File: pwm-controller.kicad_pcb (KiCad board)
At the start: 2 copper layers, 49.5 x 36.8 mm, 32 parts, among them J1 POWER, J2 LOW SIDE, J3 CTRL, J4 POWER, J5 LOW SIDE, Q1 AO3400A, Q2 AO3400A, Q3 AO3400A, Q4 AO3400A, Q5 AO3400A, Q6 AO3400A, Q7 AO3400A, U1 L78L12_SOT89, U2 MCP1416

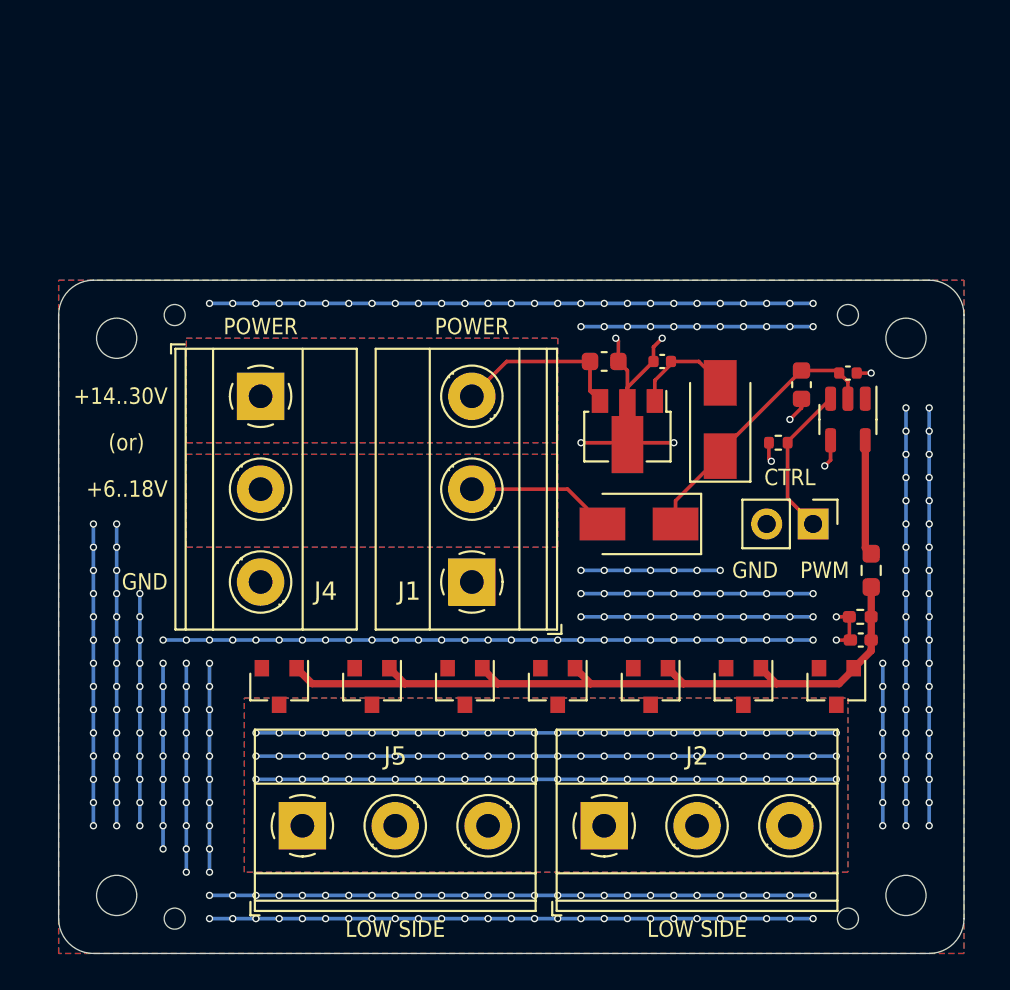
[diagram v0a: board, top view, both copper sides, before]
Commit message: ready, but some cost-saving opportunities left
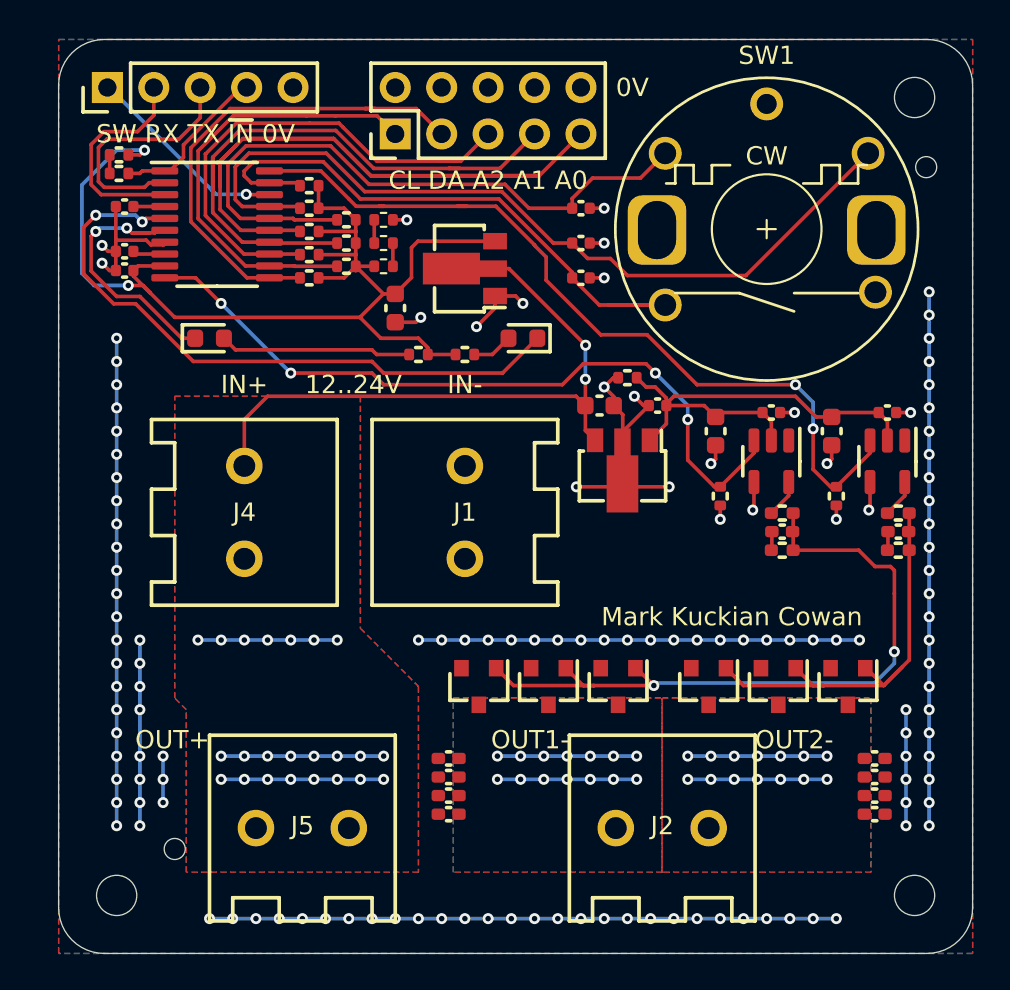
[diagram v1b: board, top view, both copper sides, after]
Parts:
- removed H3, H7: JLC, mark:JLCPCB_ToolingHole_1152_1300_1400_1650
- removed H6, H8: M2, MountingHole:MountingHole_2.2mm_M2
- removed J3: CTRL, Connector_PinHeader_2.54mm:PinHeader_1x02_P2.54mm_Vertical
- removed Q7: AO3400A, Package_TO_SOT_SMD:SOT-23
- added C10: 1u/50, Capacitor_SMD:C_0603_1608Metric, F.Cu at (117.9, 118.7)
- added C11: 100n/50, Capacitor_SMD:C_0402_1005Metric, F.Cu at (120.9, 117.7)
- added C12: 100n/50, Capacitor_SMD:C_0402_1005Metric_Pad0.74x0.62mm_HandSolder, F.Cu at (121.5, 124.2)
- added C13: 100n/50, Capacitor_SMD:C_0402_1005Metric_Pad0.74x0.62mm_HandSolder, F.Cu at (126.6, 139.7)
- added C14: 100n/50, Capacitor_SMD:C_0402_1005Metric_Pad0.74x0.62mm_HandSolder, F.Cu at (126.6, 138.7)
- added C15: 100n/50, Capacitor_SMD:C_0402_1005Metric_Pad0.74x0.62mm_HandSolder, F.Cu at (126.6, 137.7)
- added C16: 100n/50, Capacitor_SMD:C_0402_1005Metric_Pad0.74x0.62mm_HandSolder, F.Cu at (126.6, 136.7)
- added C17: 100n/50, Capacitor_SMD:C_0402_1005Metric_Pad0.74x0.62mm_HandSolder, F.Cu at (103.3, 136.7)
- added C18: 100n/50, Capacitor_SMD:C_0402_1005Metric_Pad0.74x0.62mm_HandSolder, F.Cu at (103.3, 137.7)
- added C19: 100n/50, Capacitor_SMD:C_0402_1005Metric_Pad0.74x0.62mm_HandSolder, F.Cu at (103.3, 138.7)
- added C20: 100n/50, Capacitor_SMD:C_0402_1005Metric_Pad0.74x0.62mm_HandSolder, F.Cu at (103.3, 139.7)
- added C21: 3.3n, Capacitor_SMD:C_0402_1005Metric, F.Cu at (110.5, 106.6)
- added C22: 3.3n, Capacitor_SMD:C_0402_1005Metric, F.Cu at (110.5, 108.5)
- added C23: 3.3n, Capacitor_SMD:C_0402_1005Metric, F.Cu at (110.5, 110.4)
- added C6: 3.3n, Capacitor_SMD:C_0402_1005Metric, F.Cu at (85.5, 108.9)
- added C7: 100n/50, Capacitor_SMD:C_0402_1005Metric, F.Cu at (85.5, 106.5)
- added C8: 100n/50, Capacitor_SMD:C_0402_1005Metric, F.Cu at (85.5, 110.0)
- added C9: 1u/50, Capacitor_SMD:C_0603_1608Metric, F.Cu at (100.3, 112.0)
- added H4: M2, MountingHole:MountingHole_2.2mm_M2, F.Cu at (128.7, 100.5)
- added J6: DEBUG, Connector_PinHeader_2.54mm:PinHeader_1x05_P2.54mm_Vertical, F.Cu at (84.6, 99.9)
- added J7: I2C, Connector_PinHeader_2.54mm:PinHeader_2x05_P2.54mm_Vertical, F.Cu at (100.3, 102.5)
- added R10: 4.7k, Resistor_SMD:R_0402_1005Metric, F.Cu at (95.6, 105.3)
- added R11: 4.7k, Resistor_SMD:R_0402_1005Metric, F.Cu at (95.6, 107.8)
- added R12: 120, Resistor_SMD:R_0402_1005Metric, F.Cu at (99.7, 109.7)
- added R13: 4.7k, Resistor_SMD:R_0402_1005Metric, F.Cu at (85.2, 104.6)
- added R14: 4.7k, Resistor_SMD:R_0402_1005Metric, F.Cu at (85.2, 103.6)
- added R15: 120, Resistor_SMD:R_0402_1005Metric, F.Cu at (104.1, 114.6)
- added R16: 120, Resistor_SMD:R_0402_1005Metric, F.Cu at (101.6, 114.6)
- added R17: 120, Resistor_SMD:R_0402_1005Metric_Pad0.72x0.64mm_HandSolder, F.Cu at (121.5, 123.2)
- added R18: 4.7k, Resistor_SMD:R_0402_1005Metric, F.Cu at (118.1, 122.3)
- added R19: 4.7k, Resistor_SMD:R_0402_1005Metric_Pad0.72x0.64mm_HandSolder, F.Cu at (121.5, 125.3)
- added R20: 4.7k, Resistor_SMD:R_0402_1005Metric, F.Cu at (113.0, 115.8)
- added R21: 120, Resistor_SMD:R_0402_1005Metric, F.Cu at (99.7, 108.5)
- added R22: 120, Resistor_SMD:R_0402_1005Metric, F.Cu at (99.7, 107.2)
- added R4: 4.7k, Resistor_SMD:R_0402_1005Metric, F.Cu at (97.7, 109.7)
- added R5: 4.7k, Resistor_SMD:R_0402_1005Metric, F.Cu at (95.6, 110.4)
- added R6: 4.7k, Resistor_SMD:R_0402_1005Metric, F.Cu at (97.7, 107.2)
- added R7: 4.7k, Resistor_SMD:R_0402_1005Metric, F.Cu at (95.6, 109.1)
- added R8: 4.7k, Resistor_SMD:R_0402_1005Metric, F.Cu at (95.6, 106.6)
- added R9: 4.7k, Resistor_SMD:R_0402_1005Metric, F.Cu at (97.7, 108.5)
- added SW1: EC12D1524403, mark:RotaryEncoder_Alps_EC12D_Vertical_H20mm_easy, F.Cu at (120.7, 107.7)
- added U3: STM8S003F3Px, Package_SO:TSSOP-20_4.4x6.5mm_P0.65mm, F.Cu at (90.6, 107.4)
- added U4: HT7533-1-SOT89, Package_TO_SOT_SMD:SOT-89-3, F.Cu at (104.1, 109.9)
- added U5: MCP1416, Package_TO_SOT_SMD:SOT-23-5, F.Cu at (120.9, 120.4)
- C5: value 10n -> 100n/50
- D1: value Schottky -> Green; footprint Diode_SMD:D_SMA -> LED_SMD:LED_0603_1608Metric
- D2: value Schottky -> Blue; footprint Diode_SMD:D_SMA -> LED_SMD:LED_0603_1608Metric
- J1: value POWER -> IN-; footprint TerminalBlock_Phoenix:TerminalBlock_Phoenix_MKDS-1,5-3-5.08_1x03_P5.08mm_Horizontal -> mark:ScrewTerminal_5.08P_1x02_10.16x10.16mm
- J2: value LOW SIDE -> OUT-; footprint TerminalBlock_Phoenix:TerminalBlock_Phoenix_MKDS-1,5-3-5.08_1x03_P5.08mm_Horizontal -> mark:ScrewTerminal_5.08P_1x02_10.16x10.16mm
- J4: value POWER -> IN+; footprint TerminalBlock_Phoenix:TerminalBlock_Phoenix_MKDS-1,5-3-5.08_1x03_P5.08mm_Horizontal -> mark:ScrewTerminal_5.08P_1x02_10.16x10.16mm
- J5: value LOW SIDE -> OUT+; footprint TerminalBlock_Phoenix:TerminalBlock_Phoenix_MKDS-1,5-3-5.08_1x03_P5.08mm_Horizontal -> mark:ScrewTerminal_5.08P_1x02_10.16x10.16mm
- R1: value 4.7k -> 120; footprint Resistor_SMD:R_0402_1005Metric -> Resistor_SMD:R_0402_1005Metric_Pad0.72x0.64mm_HandSolder
- R2: value 100 -> 4.7k; footprint Resistor_SMD:R_0603_1608Metric_Pad0.98x0.95mm_HandSolder -> Resistor_SMD:R_0402_1005Metric
- U1: value L78L12_SOT89 -> L78L09_SOT89
- moved H1 41.9 mm to (129.4, 104.3)
- moved D2 28.3 mm to (90.2, 113.7), turned to 0 degrees
- moved D1 12.0 mm to (107.3, 113.7)
- moved R1 7.61 mm to (127.9, 123.2)
- moved J4 6.41 mm to (92.1, 123.2)
- moved C5 6.28 mm to (127.9, 124.2)
- moved Q6 5.84 mm to (104.9, 132.7)
- moved Q5 4.57 mm to (108.7, 132.7)
- moved R2 4.49 mm to (124.5, 122.3), turned to 270 degrees
- moved R3 4.20 mm to (127.9, 125.3), turned to 180 degrees
- moved J1 3.83 mm to (104.1, 123.2)
- moved H5 3.81 mm to (88.3, 141.6)
- moved Q4 3.30 mm to (112.5, 132.7)
- moved J2 3.18 mm to (114.9, 140.5)
- moved Q3 3.17 mm to (117.5, 132.7)
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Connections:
- C1 pad 1: /24VIN -> VIN
- C2 pad 1: Net-(C2-Pad1) -> +9V
- C3 pad 1: VDD -> +9V
- C4 pad 1: VDD -> +9V
- C5 pad 1: /GATE -> /channel1/GATE
- D1 pad 1: VDD -> LED1
- D1 pad 2: /12VIN -> Net-(D1-Pad2)
- D2 pad 1: VDD -> LED2
- D2 pad 2: Net-(C2-Pad1) -> Net-(D2-Pad2)
- J1 pad 2: /12VIN -> GND
- J2 pad 1: /DRAIN -> DRAIN2
- J2 pad 2: /DRAIN -> DRAIN1
- J4 pad 1: /24VIN -> VIN
- J4 pad 2: /12VIN -> VIN
- J5 pad 1: /DRAIN -> VIN
- J5 pad 2: /DRAIN -> VIN
- Q1 pad 1: /GATE -> /channel1/GATE
- Q1 pad 3: /DRAIN -> DRAIN1
- Q2 pad 1: /GATE -> /channel1/GATE
- Q2 pad 3: /DRAIN -> DRAIN1
- Q3 pad 1: /GATE -> /channel1/GATE
- Q3 pad 3: /DRAIN -> DRAIN1
- Q4 pad 1: /GATE -> /channel2/GATE
- Q4 pad 3: /DRAIN -> DRAIN2
- Q5 pad 1: /GATE -> /channel2/GATE
- Q5 pad 3: /DRAIN -> DRAIN2
- Q6 pad 1: /GATE -> /channel2/GATE
- Q6 pad 3: /DRAIN -> DRAIN2
- R1 pad 1: /CTRL -> /channel1/GATE
- R1 pad 2: GND -> /channel1/GATE_DRV
- R2 pad 1: /GATE -> PWM1
- R2 pad 2: /GATE_DRV -> GND
- R3 pad 1: GND -> /channel1/GATE
- R3 pad 2: /GATE -> GND
- U1 pad 1: Net-(C2-Pad1) -> +9V
- U1 pad 3: /24VIN -> VIN
- U2 pad 2: VDD -> +9V
- U2 pad 3: /CTRL -> PWM1
- U2 pad 5: /GATE_DRV -> /channel1/GATE_DRV
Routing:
- net GND: track 336.6 -> 175.6 mm, vias 274 -> 132
- net /DRAIN: track 95.2 -> 0.00 mm, vias 78 -> 0
- net +3V3: track 0.00 -> 62.0 mm, vias 0 -> 2
- net VIN: track 0.00 -> 59.6 mm, vias 0 -> 25
- net SADD0: track 0.00 -> 55.7 mm
- net RE_Q: track 0.00 -> 46.0 mm
- net PWM1: track 0.00 -> 45.3 mm, vias 0 -> 2
- net /GATE: track 42.1 -> 0.00 mm
- net PWM2: track 0.00 -> 41.3 mm, vias 0 -> 4
- net /channel2/GATE: track 0.00 -> 39.1 mm, vias 0 -> 2
- net RE_I: track 0.00 -> 35.9 mm
- net LED1: track 0.00 -> 35.3 mm, vias 0 -> 2
- net RE_B: track 0.00 -> 33.3 mm
- net SADD1: track 0.00 -> 32.8 mm
- net SADD2: track 0.00 -> 27.9 mm
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- added copper zone on B.Cu, net DRAIN1
- added copper zone on F.Cu, net DRAIN1
- added copper zone on B.Cu, net DRAIN2
- added copper zone on F.Cu, net DRAIN2
- added copper zone on B.Cu, net VIN
- added copper zone on F.Cu, net VIN
- removed copper zone on B.Cu, net /12VIN
- removed copper zone on F.Cu, net /12VIN
- removed copper zone on B.Cu, net /24VIN
- removed copper zone on F.Cu, net /24VIN
- removed copper zone on B.Cu, net /DRAIN
- removed copper zone on F.Cu, net /DRAIN
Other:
- board size 49.5 x 36.8 mm -> 50 x 50 mm
- net class Default: via_dia 0.4 -> 0.6; via_drill 0.25 -> 0.3
- net class Gate removed
- net class Power removed
- net class Signal removed
- rule via_min_drill: 0.25 -> 0.3
- rule via_min_size: 0.4 -> 0.6
- board text added: "0V"
- board text added: "10A should cause up to 100mV noise on GND. Slotting GND plane to reduce noise in digital section."
- board text added: "12..24V"
- board text added: "CL DA A2 A1 A0"
- board text added: "Mark Kuckian Cowan"
- board text added: "SW RX TX ~IN~ 0V"
- board text removed: "(or)"
- board text removed: "+14..30V"
- board text removed: "+6..18V"
- board text removed: "GND"
- board text removed: "PWM"

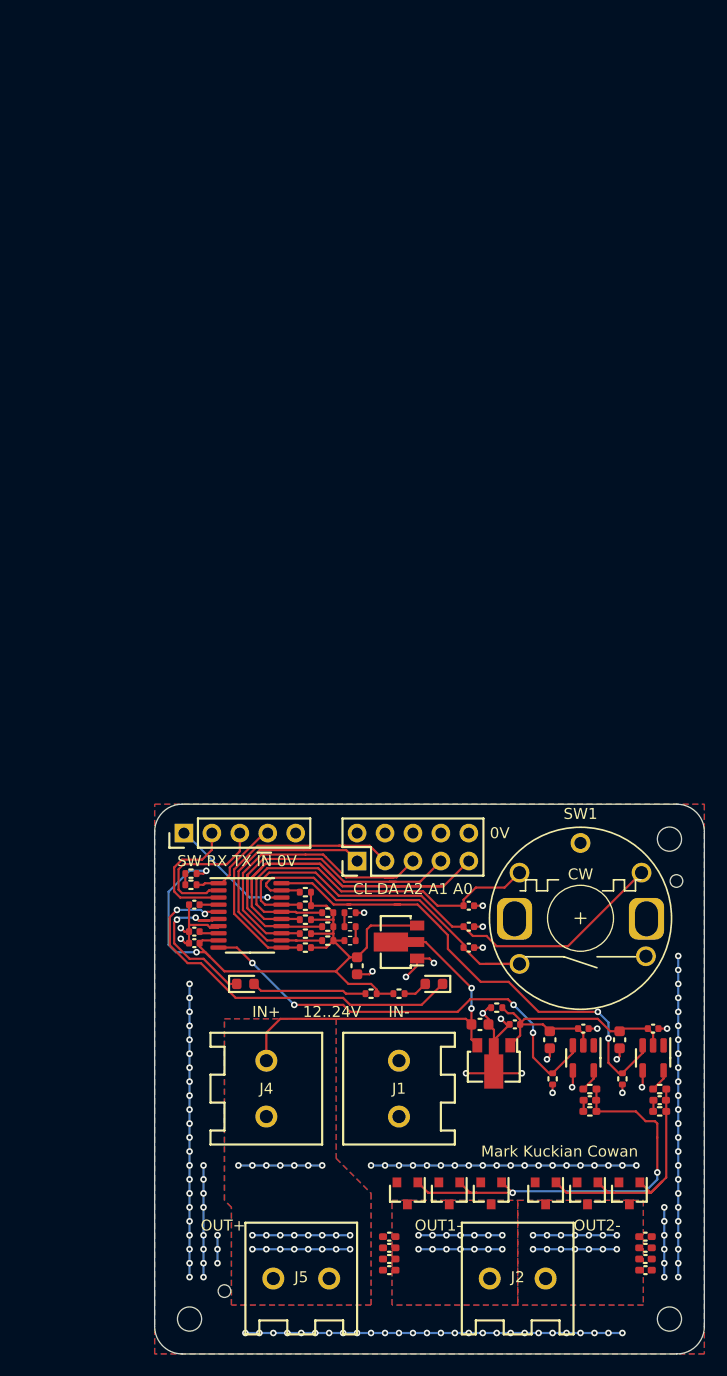
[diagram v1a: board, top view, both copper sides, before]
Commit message: dual channel, cheaper (jellybean gate driver)
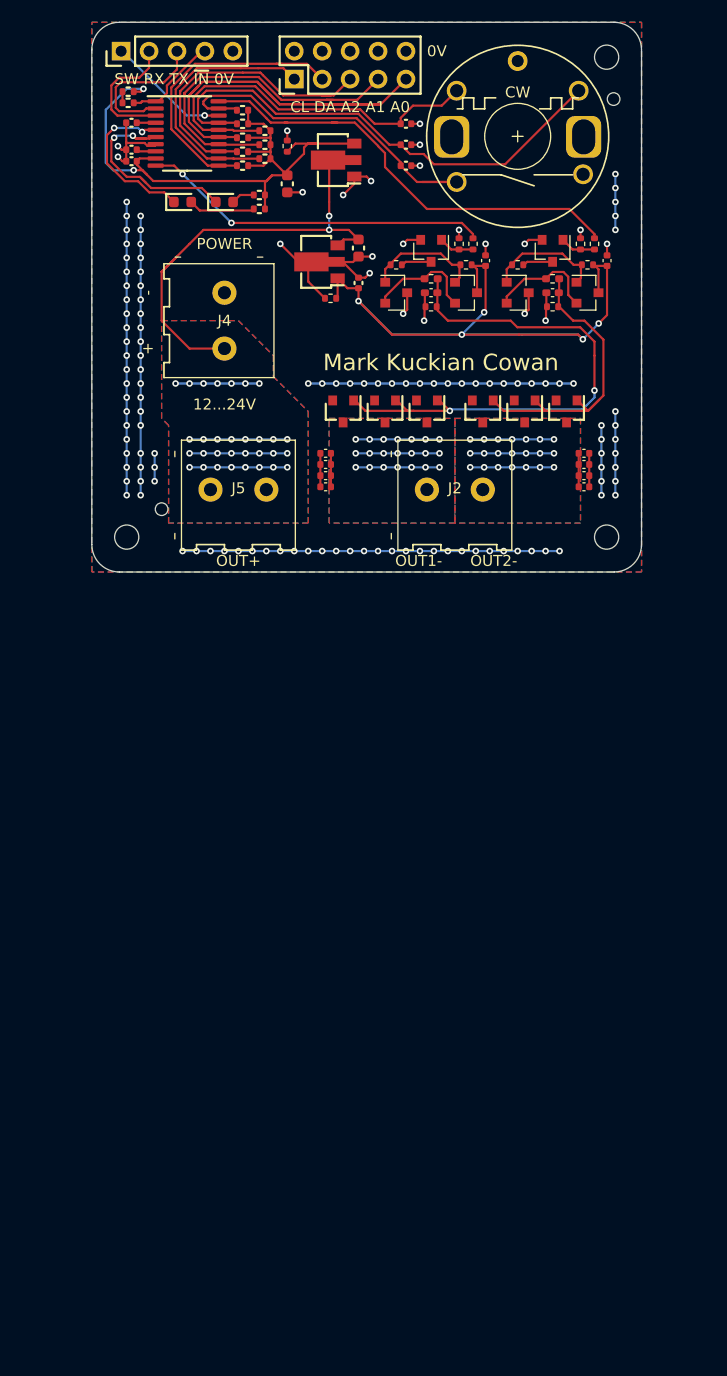
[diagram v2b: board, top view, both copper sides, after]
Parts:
- removed C11: 100n/50, Capacitor_SMD:C_0402_1005Metric
- removed C12: 100n/50, Capacitor_SMD:C_0402_1005Metric_Pad0.74x0.62mm_HandSolder
- removed J1: IN-, mark:ScrewTerminal_5.08P_1x02_10.16x10.16mm
- removed R21, R22: 120, Resistor_SMD:R_0402_1005Metric
- removed U2, U5: MCP1416, Package_TO_SOT_SMD:SOT-23-5
- added Q10: MMBT5551, Package_TO_SOT_SMD:SOT-23, F.Cu at (110.2, 50.8)
- added Q11: MMBT5551, Package_TO_SOT_SMD:SOT-23, F.Cu at (107.1, 47.0)
- added Q12: MMBT5401, Package_TO_SOT_SMD:SOT-23, F.Cu at (103.9, 50.8)
- added Q7: MMBT5551, Package_TO_SOT_SMD:SOT-23, F.Cu at (121.3, 50.8)
- added Q8: MMBT5551, Package_TO_SOT_SMD:SOT-23, F.Cu at (118.1, 47.0)
- added Q9: MMBT5401, Package_TO_SOT_SMD:SOT-23, F.Cu at (114.9, 50.8)
- added R23: 4.7k, Resistor_SMD:R_0402_1005Metric, F.Cu at (110.2, 48.3)
- added R24: 120, Resistor_SMD:R_0402_1005Metric_Pad0.72x0.64mm_HandSolder, F.Cu at (107.1, 49.5)
- added R25: 4.7k, Resistor_SMD:R_0402_1005Metric, F.Cu at (103.9, 48.3)
- added R27: 4.7k, Resistor_SMD:R_0402_1005Metric, F.Cu at (107.1, 52.1)
- added R28: 1k, Resistor_SMD:R_0402_1005Metric, F.Cu at (110.9, 46.4)
- added R29: 4.7k, Resistor_SMD:R_0402_1005Metric, F.Cu at (109.6, 46.4)
- C10: value 1u/50 -> 100n/50; footprint Capacitor_SMD:C_0603_1608Metric -> Capacitor_SMD:C_0402_1005Metric
- C13, C14, C15, C16, C17, C18, C19, C20, C5: footprint Capacitor_SMD:C_0402_1005Metric_Pad0.74x0.62mm_HandSolder -> Capacitor_SMD:C_0402_1005Metric
- C3: value 1u/50 -> 100n/50; footprint Capacitor_SMD:C_0603_1608Metric -> Capacitor_SMD:C_0402_1005Metric_Pad0.74x0.62mm_HandSolder
- C4: footprint Capacitor_SMD:C_0402_1005Metric -> Capacitor_SMD:C_0402_1005Metric_Pad0.74x0.62mm_HandSolder
- J4: value IN+ -> POWER
- R1, R17: value 120 -> 4.7k; footprint Resistor_SMD:R_0402_1005Metric_Pad0.72x0.64mm_HandSolder -> Resistor_SMD:R_0402_1005Metric
- R12: value 120 -> 4.7k
- R19: value 4.7k -> 1k; footprint Resistor_SMD:R_0402_1005Metric_Pad0.72x0.64mm_HandSolder -> Resistor_SMD:R_0402_1005Metric
- R2: value 4.7k -> 120; footprint Resistor_SMD:R_0402_1005Metric -> Resistor_SMD:R_0402_1005Metric_Pad0.72x0.64mm_HandSolder
- R3: footprint Resistor_SMD:R_0402_1005Metric_Pad0.72x0.64mm_HandSolder -> Resistor_SMD:R_0402_1005Metric
- moved R17 90.1 mm to (94.0, 37.5), turned to 270 degrees
- moved R19 78.9 mm to (121.9, 46.4), turned to 90 degrees
- moved R3 78.1 mm to (114.9, 48.3), turned to 0 degrees
- moved C5 78.0 mm to (112.0, 47.9), turned to 90 degrees
- moved R1 75.3 mm to (121.3, 48.3)
- moved D1 74.7 mm to (84.5, 42.5), turned to 0 degrees
- moved U1 74.6 mm to (96.9, 48.0), turned to 180 degrees
- moved R16 73.4 mm to (91.4, 41.9)
- moved R2 73.0 mm to (118.1, 49.5), turned to 0 degrees
- moved R15 72.5 mm to (91.4, 43.2), turned to 0 degrees
- moved J2 72.0 mm to (109.2, 68.7)
- moved J5 72.0 mm to (89.5, 68.7)
- moved C18 71.5 mm to (97.5, 66.4)
- moved C19 71.5 mm to (97.5, 67.4)
- moved C17 71.5 mm to (97.5, 65.4)
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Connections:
- C3 pad 1: +9V -> /channel1/GATE
- C4 pad 1: +9V -> /channel2/GATE
- C5 pad 1: /channel1/GATE -> +9V
- J4 pad 1: VIN -> GND
- R1 pad 1: /channel1/GATE -> +9V
- R1 pad 2: /channel1/GATE_DRV -> Net-(Q7-Pad1)
- R12 pad 1: Net-(R12-Pad1) -> GND
- R12 pad 2: +3V3 -> +9V
- R17 pad 1: /channel2/GATE -> GND
- R17 pad 2: /channel2/GATE_DRV -> +3V3
- R18 pad 1: PWM2 -> /channel1/GATE
- R19 pad 1: /channel2/GATE -> Net-(Q8-Pad1)
- R19 pad 2: GND -> PWM1
- R2 pad 1: PWM1 -> Net-(Q7-Pad2)
- R2 pad 2: GND -> /channel1/GATE
- R20 pad 1: GND -> Net-(Q8-Pad1)
- R20 pad 2: +9V -> GND
- R3 pad 1: /channel1/GATE -> Net-(Q7-Pad1)
- R3 pad 2: GND -> Net-(Q8-Pad3)
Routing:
- net +9V: track 26.4 -> 71.7 mm, vias 0 -> 5
- net LED1: track 35.3 -> 15.0 mm
- net VIN: track 59.6 -> 77.6 mm, vias 25 -> 33
- net GND: track 175.6 -> 190.3 mm, vias 132 -> 133
- net Net-(Q7-Pad1): track 0.00 -> 10.7 mm
- net Net-(Q10-Pad1): track 0.00 -> 10.7 mm
- net DRAIN2: track 15.2 -> 25.9 mm, vias 14 -> 21
- net DRAIN1: track 15.2 -> 25.9 mm, vias 14 -> 21
- net /channel2/GATE: track 39.1 -> 49.4 mm
- net Net-(Q10-Pad2): track 0.00 -> 10.0 mm
- net Net-(Q7-Pad2): track 0.00 -> 10.0 mm
- net PWM2: track 41.3 -> 31.8 mm, vias 4 -> 2
- net Net-(D2-Pad2): track 10.5 -> 2.14 mm
- net /channel1/GATE: track 23.8 -> 28.6 mm
- net LED2: track 14.6 -> 19.1 mm
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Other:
- board text removed: "12..24V"

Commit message: simulation provided many improvements, now aboutto switch to 5v single-rail for all control stuff
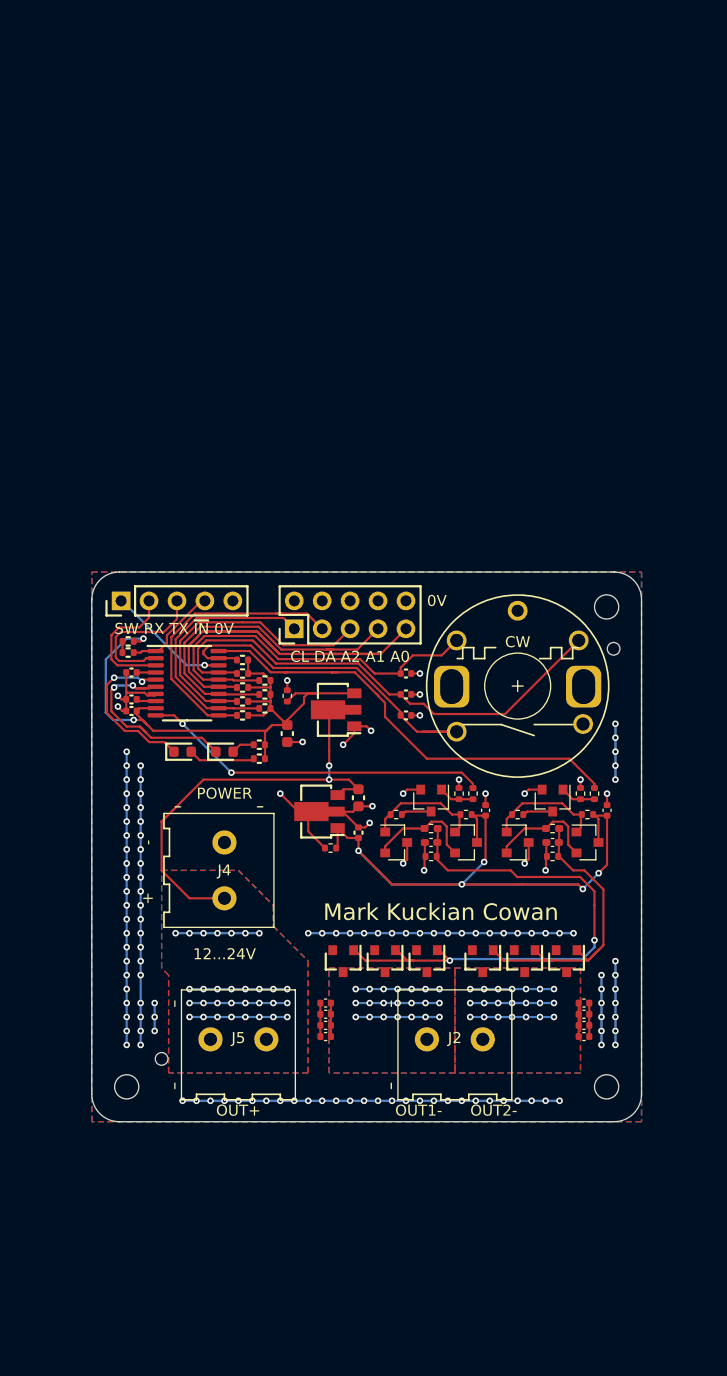
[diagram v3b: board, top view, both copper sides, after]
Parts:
- moved C1 50.0 mm to (100.5, 96.7)
- moved C10 50.0 mm to (123.1, 97.9)
- moved C21 50.0 mm to (104.8, 85.4)
- moved C5 50.0 mm to (112.0, 97.9)
- moved C6 50.0 mm to (79.8, 87.8)
- moved C9 50.0 mm to (94.0, 90.9)
- moved R1 50.0 mm to (121.3, 98.3)
- moved R12 50.0 mm to (97.9, 101.3)
- moved R13 50.0 mm to (79.5, 83.5)
- moved R15 50.0 mm to (91.4, 93.2)
- moved R19 50.0 mm to (121.9, 96.4)
- moved R20 50.0 mm to (120.7, 96.4)
- moved R23 50.0 mm to (110.2, 98.3)
- moved R25 50.0 mm to (103.9, 98.3)
- moved R28 50.0 mm to (110.9, 96.4)
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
